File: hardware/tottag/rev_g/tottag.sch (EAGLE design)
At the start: 154 parts, among them J1 MICRO_USB_B_HIROSE_ZX62-B-5PA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, J2 CON_MICRO_SDDM3AT-SF-PEJM5, J3 BAT_HOLE, J4 TC2030-JLINK-NL, J5 TC2030-JLINK-NL, T1 HHM1595A1, U1 DW1000, U10 STM32F091CC, U11 AB1815-T3, U2 FT232RQ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

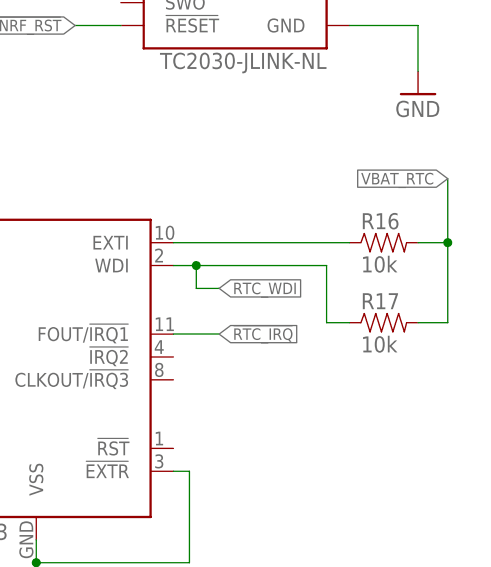
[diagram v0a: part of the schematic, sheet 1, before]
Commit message: rev_g: tie RTC signals WDI, EXTI to GND
According to the datasheet,

> [WDI, EXTI] must not be left floating or the RTC may consume higher current.
> Instead, it must be connected directly to either VCC or VSS if not used.

These used to be tied high to the RTC battery, but that drained the
battery. Instead, tie them to the RTC's VSS (the GND net).
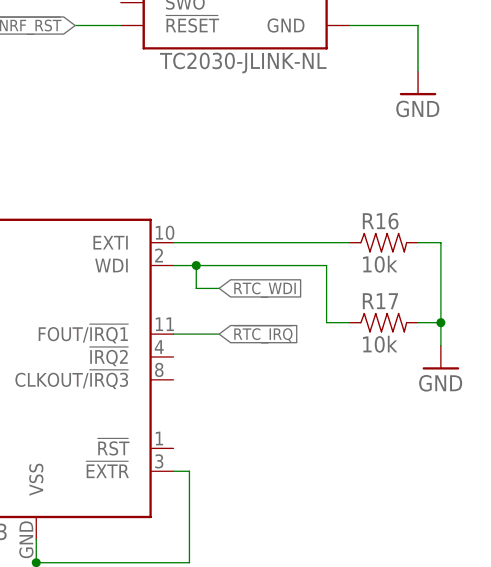
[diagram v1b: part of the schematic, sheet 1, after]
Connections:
- net GND: now also R16.2, R17.2
- net VBAT_RTC: no longer R16.2, R17.2
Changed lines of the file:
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@@
 <setting verticaltext="up"/>
 </settings>
-<grid distance="0.1" unitdist="inch" unit="inch" style="lines" multiple="1" display="no" altdistance="0.01" altunitdist="inch" altunit="inch"/>
+<grid distance="0.1" unitdist="inch" unit="inch" style="lines" multiple="1" display="yes" altdistance="0.01" altunitdist="inch" altunit="inch"/>
 <layers>
 <layer number="1" name="Top" color="4" fill="1" visible="no" active="no"/>
@@
 <part name="C71" library="passives" deviceset="CAPACITOR" device="0402_CAP" value="10uF"/>
 <part name="U4" library="regulators" deviceset="XCL206" device="B"/>
+<part name="GND2" library="supply1" library_urn="urn:adsk.eagle:library:371" deviceset="GND" device=""/>
 </parts>
 <sheets>
@@
 <attribute name="VALUE" x="183.896" y="125.476" size="1.778" layer="96" rot="R180"/>
 </instance>
+<instance part="GND2" gate="1" x="248.92" y="104.14" smashed="yes">
+<attribute name="VALUE" x="246.38" y="101.6" size="1.778" layer="96"/>
+</instance>
 </instances>
 <busses>
@@
 <wire x1="220.98" y1="82.55" x2="203.962" y2="82.55" width="0.1524" layer="91"/>
 <junction x="203.962" y="82.55"/>
+</segment>
+<segment>
+<pinref part="R17" gate="G$1" pin="2"/>
+<wire x1="246.38" y1="109.22" x2="248.92" y2="109.22" width="0.1524" layer="91"/>
+<pinref part="GND2" gate="1" pin="GND"/>
+<wire x1="248.92" y1="109.22" x2="248.92" y2="106.68" width="0.1524" layer="91"/>
+<pinref part="R16" gate="G$1" pin="2"/>
+<wire x1="246.38" y1="118.11" x2="248.92" y2="118.11" width="0.1524" layer="91"/>
+<wire x1="248.92" y1="118.11" x2="248.92" y2="109.22" width="0.1524" layer="91"/>
+<junction x="248.92" y="109.22"/>
 </segment>
 </net>
@@
 <junction x="173.482" y="127"/>
 </segment>
-<segment>
-<wire x1="249.682" y1="109.22" x2="249.682" y2="118.11" width="0.1524" layer="91"/>
-<wire x1="249.682" y1="118.11" x2="249.682" y2="125.222" width="0.1524" layer="91"/>
-<label x="249.682" y="125.222" size="1.27" layer="95" rot="R180" xref="yes"/>
-<pinref part="R16" gate="G$1" pin="2"/>
-<wire x1="246.38" y1="118.11" x2="249.682" y2="118.11" width="0.1524" layer="91"/>
-<junction x="249.682" y="118.11"/>
-<pinref part="R17" gate="G$1" pin="2"/>
-<wire x1="246.38" y1="109.22" x2="249.682" y2="109.22" width="0.1524" layer="91"/>
-</segment>
-</net>
+</net>

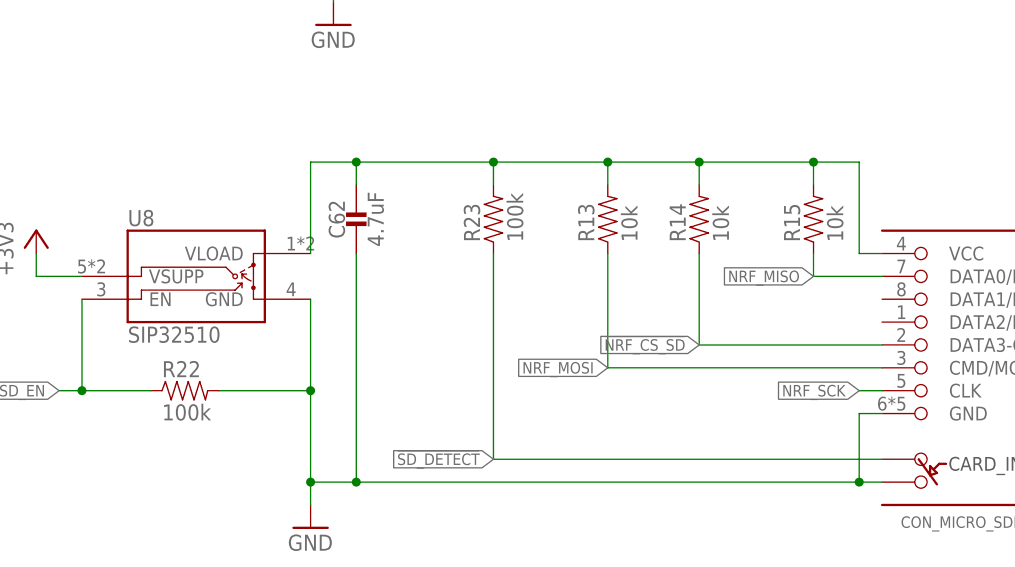
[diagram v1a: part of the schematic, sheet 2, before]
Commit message: rev_g: SD card SPI pullups 10k -> 100k
To reduce leakage through the SD Card, increase the pullups on the SPI lines
from 10k to 100k. This now matches the pullup already in use for the card
present detection.

Resistors renumbered as a result:

> R16 : 10k   0402_RES           => R13 : 10k   0402_RES
> R17 : 10k   0402_RES           => R14 : 10k   0402_RES
> R18 : 10k   0402_RES           => R15 : 10k   0402_RES
>
> R19 : 11k 1%   0402_RES        => R16 : 11k 1%   0402_RES
> R20 : 11k   0402_RES           => R17 : 11k   0402_RES
>
> R21 : 16k   0402_RES           => R18 : 16k   0402_RES
>
> R22 : 100k   0402_RES          => R19 : 100k   0402_RES
> R23 : 100k   0402_RES          => R20 : 100k   0402_RES
> R13 : 100k   0402_RES          => R21 : 100k   0402_RES
> R14 : 100k   0402_RES          => R22 : 100k   0402_RES
> R15 : 100k   0402_RES          => R23 : 100k   0402_RES
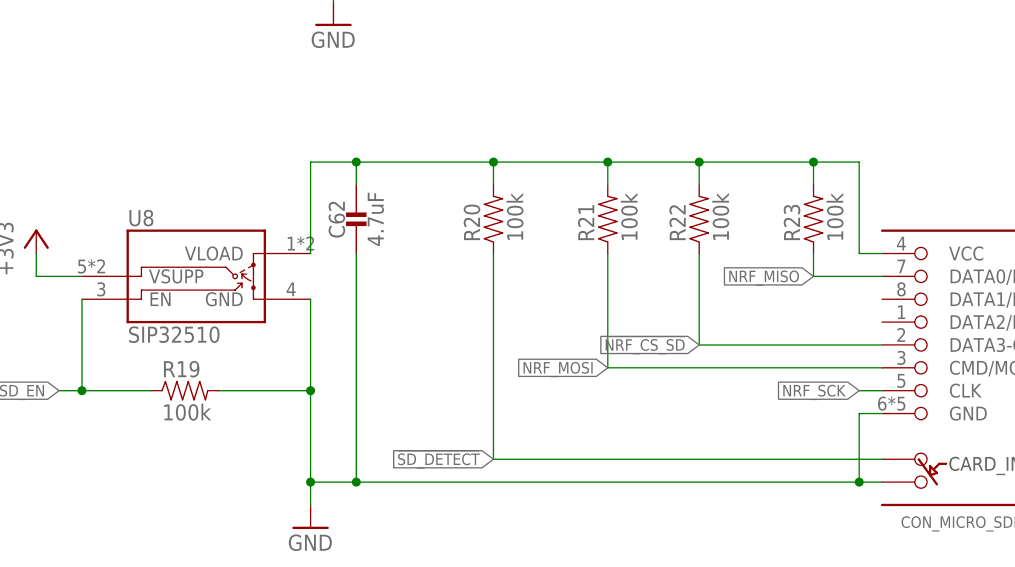
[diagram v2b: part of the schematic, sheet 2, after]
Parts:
- R13, R14, R15: DIGIKEY (none) -> 311-10KJRCT-ND; MPN (none) -> RC0402JR-0710KL
- R16: value 10k -> 11k 1%; DIGIKEY 311-10KJRCT-ND -> (none); MPN RC0402JR-0710KL -> (none)
- R17: value 10k -> 11k; DIGIKEY 311-10KJRCT-ND -> (none); MPN RC0402JR-0710KL -> (none)
- R18: value 10k -> 16k; DIGIKEY 311-10KJRCT-ND -> (none); MPN RC0402JR-0710KL -> (none)
- R19: value 11k 1% -> 100k
- R20: value 11k -> 100k
- R21: value 16k -> 100k
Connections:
- net !NRF_CS_RTC: now also R15.1; no longer R18.1
- net !NRF_CS_SD: now also R22.1; no longer R14.1
- net !SD_DETECT: now also R20.1; no longer R23.1
- net GND: now also R13.2, R14.2, R16.1, R19.2; no longer R16.2, R19.1, R20.2, R22.2
- net N$12: now also R18.2; no longer R21.2
- net N$16: now also R18.1; no longer R21.1
- net N$21: now also R16.2; no longer R19.2
- net N$22: now also R17.1; no longer R20.1
- net N$43: now also R13.1; no longer R16.1
- net N$55: now also R20.2, R21.2, R22.2; no longer R13.2, R14.2, R15.2
- net NRF_MISO: now also R23.1; no longer R15.1
- net NRF_MOSI: now also R21.1; no longer R13.1
- net RTC_WDI: now also R14.1; no longer R17.1
- net SD_EN: now also R19.1; no longer R22.1
- net VBAT_RTC: now also R15.2; no longer R18.2
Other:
- moved on the sheet: R22, R23

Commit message: rev_g: add note with battery part number
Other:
- note added: ""Standard" battery is PKCELL LP803860 1528-1857-ND"
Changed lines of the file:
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@@
 for optimal performance</text>
 <text x="222.758" y="140.97" size="1.778" layer="98" rot="R180" align="bottom-center">90 Ohm</text>
+<text x="160.782" y="181.61" size="1.778" layer="98">"Standard" battery is
+PKCELL LP803860
+1528-1857-ND</text>
 </plain>
 <instances>

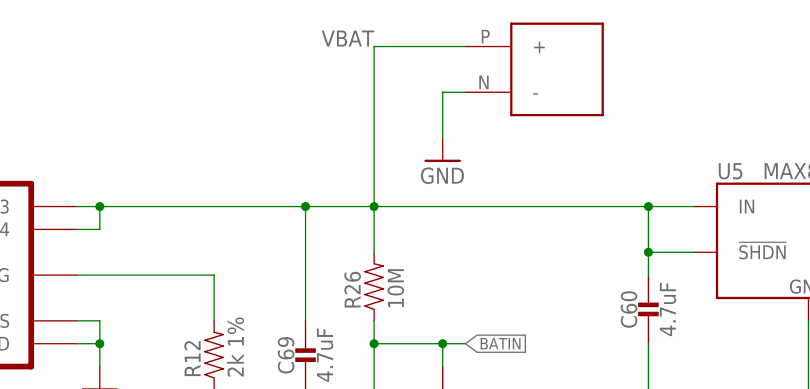
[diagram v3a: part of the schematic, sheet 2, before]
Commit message: rev_g: [WIP] Relayot for mass-manufacture case
 - Needs to be slightly more square and less rectangualar overall
 - Add "wings" that go around screw stands
 - Do not move any antennas (yet, BLE can move to a better spot)
 - Move components off the bottom to let battery sit flush

This does the major work, the detail work is still to go
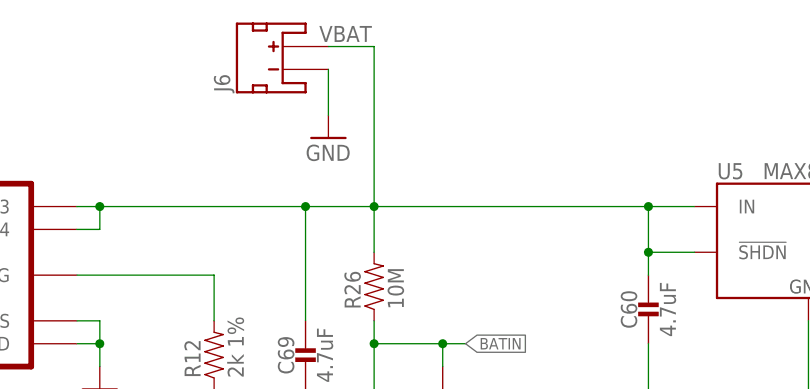
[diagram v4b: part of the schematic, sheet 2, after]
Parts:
- removed J3: BAT_HOLE, connector:BAT_HOLE
- added J6: (no value), SparkFun-Connectors:JST_2MM_MALE
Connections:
- net GND: now also J6.-; no longer J3.-
- net VBAT: now also J6.+; no longer J3.+
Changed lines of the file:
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@@
 <part name="SUPPLY2" library="supply1" library_urn="urn:adsk.eagle:library:371" deviceset="GND" device=""/>
 <part name="J1" library="connector" deviceset="MICRO_USB_B_HIROSE_ZX62-B-5PA(11)" device=""/>
-<part name="J3" library="connector" deviceset="BAT_HOLE" device=""/>
 <part name="SUPPLY8" library="supply1" library_urn="urn:adsk.eagle:library:371" deviceset="GND" device=""/>
 <part name="TP2" library="testpad" library_urn="urn:adsk.eagle:library:385" deviceset="TP" device="TP06SQ" package3d_urn="urn:adsk.eagle:package:27952/1"/>
@@
 <part name="U4" library="regulators" deviceset="XCL206" device="B"/>
 <part name="GND2" library="supply1" library_urn="urn:adsk.eagle:library:371" deviceset="GND" device=""/>
+<part name="J6" library="SparkFun-Connectors" library_urn="urn:adsk.eagle:library:513" deviceset="JST_2MM_MALE" device="" package3d_urn="urn:adsk.eagle:package:38042/1"/>
 </parts>
 <sheets>
@@
 for optimal performance</text>
 <text x="222.758" y="140.97" size="1.778" layer="98" rot="R180" align="bottom-center">90 Ohm</text>
-<text x="160.782" y="181.61" size="1.778" layer="98">"Standard" battery is
+<text x="112.522" y="179.07" size="1.778" layer="98" align="center-right">"Standard" battery is
 PKCELL LP803860
 1528-1857-ND</text>
@@
 <attribute name="VALUE" x="12.7" y="144.78" size="1.778" layer="95" rot="MR0"/>
 </instance>
-<instance part="J3" gate="G$1" x="152.4" y="177.8" smashed="yes" rot="MR0"/>
-<instance part="SUPPLY8" gate="1" x="139.7" y="167.64" smashed="yes">
-<attribute name="VALUE" x="137.16" y="165.1" size="1.778" layer="96"/>
+<instance part="SUPPLY8" gate="1" x="127" y="170.18" smashed="yes">
+<attribute name="VALUE" x="124.46" y="167.64" size="1.778" layer="96"/>
 </instance>
 <instance part="U5" gate="G$1" x="180.34" y="160.02" smashed="yes">
@@
 <attribute name="NAME" x="235.1786" y="158.75" size="1.778" layer="95" rot="R270"/>
 <attribute name="VALUE" x="230.378" y="158.75" size="1.778" layer="96" rot="R270"/>
+</instance>
+<instance part="J6" gate="G$1" x="121.92" y="177.8" smashed="yes" rot="R90">
+<attribute name="NAME" x="116.078" y="175.26" size="1.778" layer="95" rot="R90"/>
 </instance>
 </instances>
@@
 <segment>
 <pinref part="SUPPLY8" gate="1" pin="GND"/>
-<wire x1="139.7" y1="170.18" x2="139.7" y2="175.26" width="0.1524" layer="91"/>
-<pinref part="J3" gate="G$1" pin="-"/>
-<wire x1="139.7" y1="175.26" x2="142.24" y2="175.26" width="0.1524" layer="91"/>
+<wire x1="127" y1="172.72" x2="127" y2="177.8" width="0.1524" layer="91"/>
+<pinref part="J6" gate="G$1" pin="-"/>
 </segment>
 <segment>
@@
 <junction x="162.56" y="162.56"/>
 <wire x1="132.08" y1="180.34" x2="132.08" y2="162.56" width="0.1524" layer="91"/>
-<pinref part="J3" gate="G$1" pin="+"/>
-<wire x1="132.08" y1="180.34" x2="142.24" y2="180.34" width="0.1524" layer="91"/>
+<wire x1="132.08" y1="180.34" x2="127" y2="180.34" width="0.1524" layer="91"/>
 <pinref part="U5" gate="G$1" pin="IN"/>
 <wire x1="162.56" y1="162.56" x2="167.64" y2="162.56" width="0.1524" layer="91"/>
@@
 <wire x1="101.6" y1="160.02" x2="101.6" y2="162.56" width="0.1524" layer="91"/>
 <junction x="101.6" y="162.56"/>
-<label x="132.08" y="180.34" size="1.778" layer="95" rot="MR0"/>
+<label x="131.826" y="180.848" size="1.778" layer="95" rot="MR0"/>
 <pinref part="C69" gate="G$1" pin="1"/>
 <wire x1="124.46" y1="162.56" x2="124.46" y2="149.86" width="0.1524" layer="91"/>
 <junction x="124.46" y="162.56"/>
-</segment>
-</net>
+<pinref part="J6" gate="G$1" pin="+"/>
+</segment>
+</net>

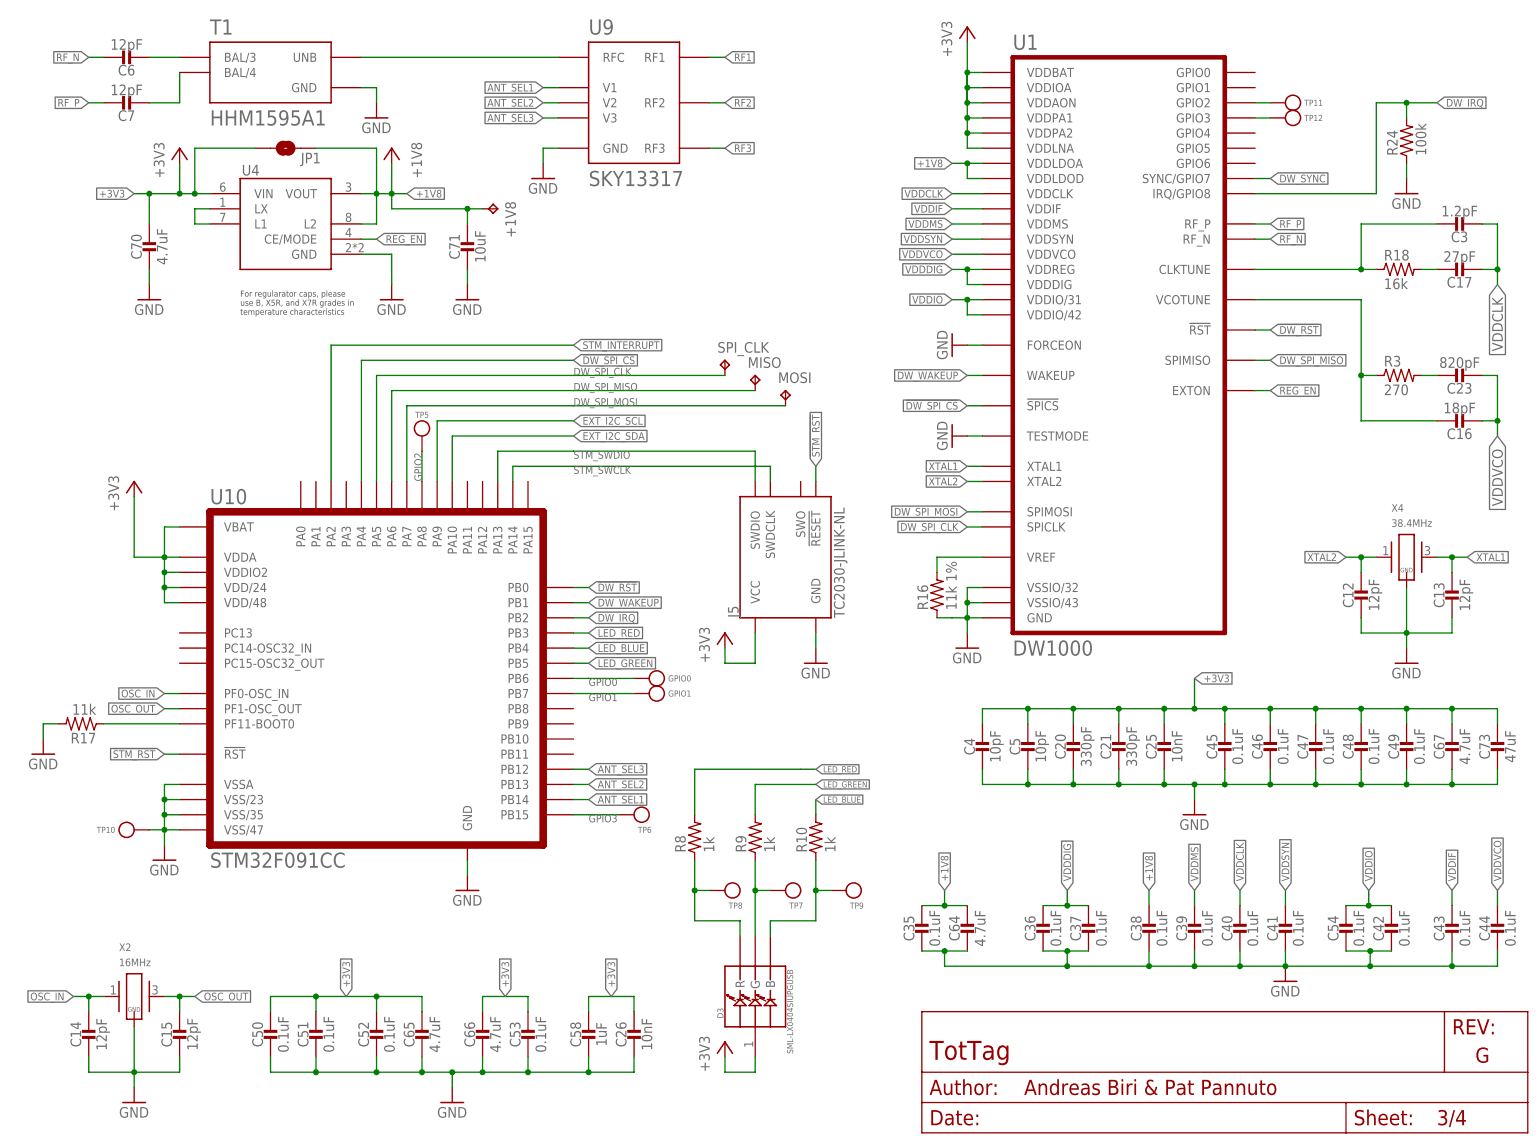
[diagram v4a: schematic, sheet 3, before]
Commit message: rev_g: [WIP] Add jlink headers to bottom side
In the 'installed' configuration in the case, it will be easier to
get to the bottom side, so add pads there too.
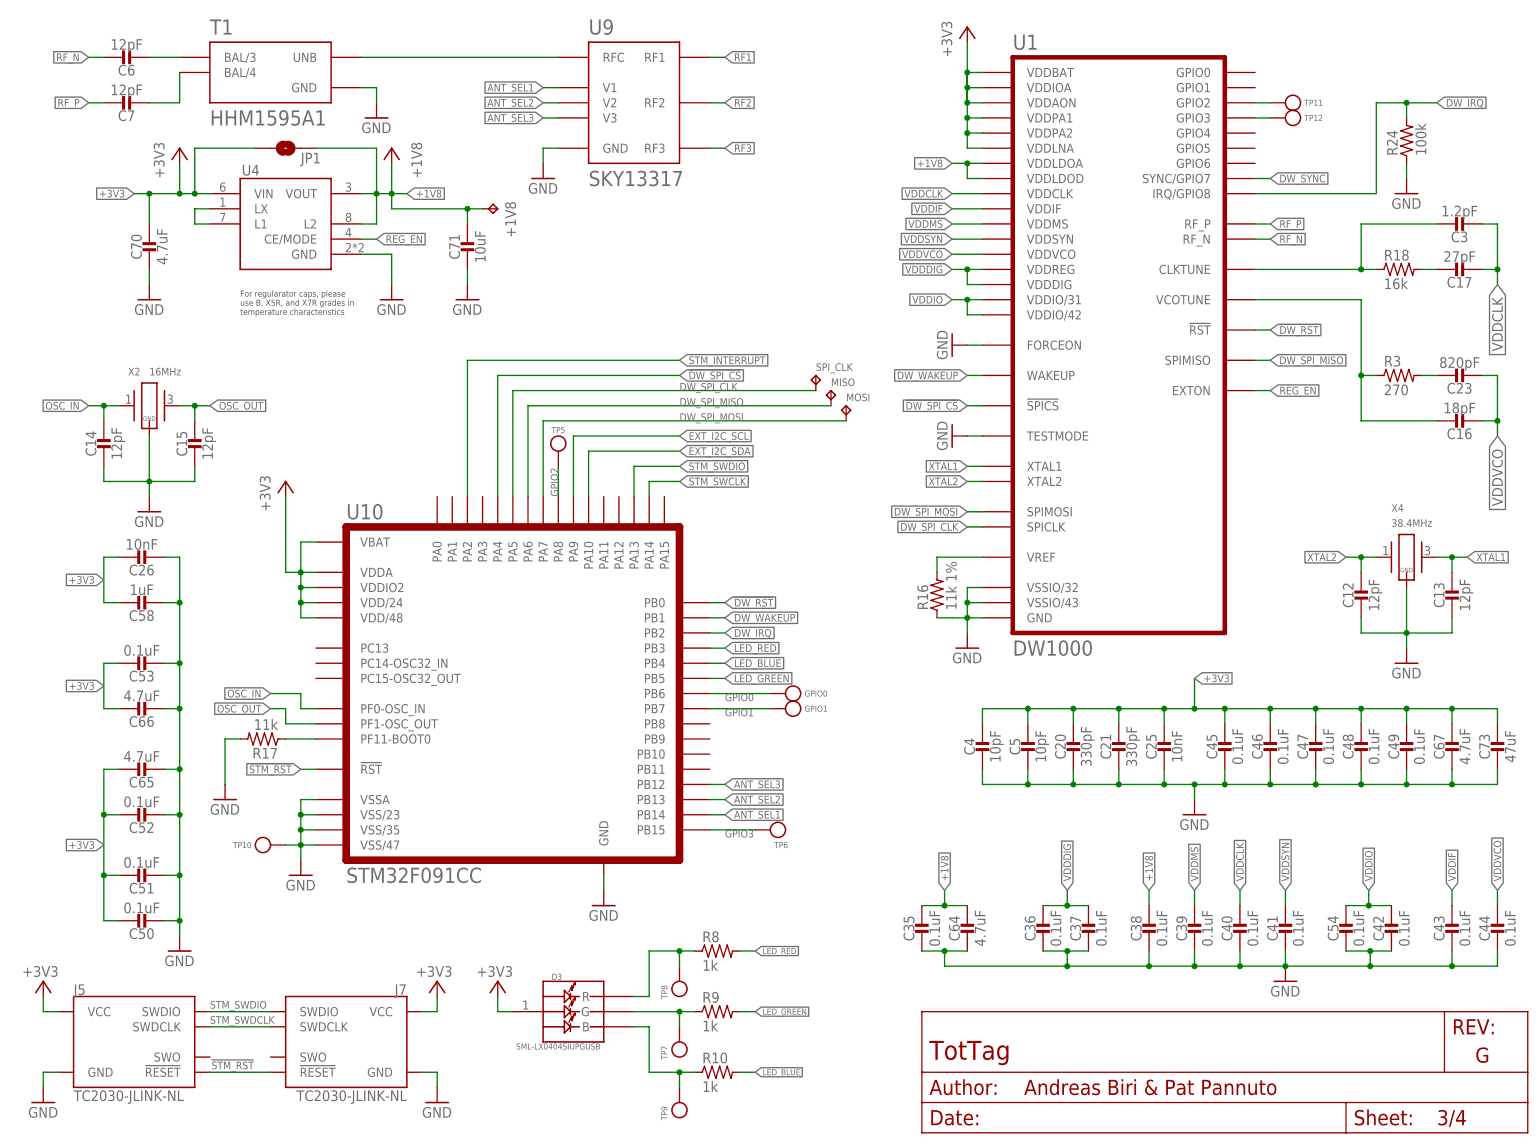
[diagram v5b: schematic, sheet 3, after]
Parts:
- added J3, J7: TC2030-JLINK-NL, connector:TC2030-JLINK-NL
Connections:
- new net STM_SWDCLK: J5.SWDCLK, J7.SWDCLK
- net !NRF_RST: now also J3.!RESET
- net !STM_RST: now also J7.!RESET
- net +3V3: now also J3.VCC, J7.VCC
- net GND: now also J3.GND, J7.GND
- net NRF_SWDCLK: now also J3.SWDCLK
- net NRF_SWDIO: now also J3.SWDIO
- net STM_SWCLK: no longer J5.SWDCLK
- net STM_SWDIO: now also J7.SWDIO
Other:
- note added: "2x Programming header (top/bot)"
- note added: "x2 (top/bottom)"
- moved on the sheet: C14, C15, C26, C50, C51, C52, C53, C58, C65, C66, D3, GPIO0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
